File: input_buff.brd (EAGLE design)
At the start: 100 x 80 mm, 32 parts, among them X1 057-010-1, X2 057-016-1

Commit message: remains drc pass.
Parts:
- moved TP8 65.9 mm to (15.9, 2.54)
- moved TP7 63.1 mm to (14.6, 3.81)
- moved TP6 61.9 mm to (15.9, 5.08)
- moved TP5 59.1 mm to (14.6, 6.35)
- moved TP4 58.0 mm to (15.9, 7.62)
- moved TP3 55.3 mm to (14.6, 8.89)
- moved TP2 54.3 mm to (15.9, 10.2)
- moved TP1 51.7 mm to (14.6, 11.4)
- moved R3 14.8 mm to (19.7, 26.7)
- moved TP18 11.1 mm to (12.1, 26.7)
- moved TP17 6.25 mm to (31.1, 26.7)
- moved LED1 3.59 mm to (26.7, 26.7), turned to 180 degrees
- moved TP16 2.84 mm to (33.0, 3.81)
- moved R1 1.42 mm to (14.6, 20.3)
- moved R2 1.42 mm to (14.6, 15.2)
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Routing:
- net 1V8: track 6.19 -> 29.9 mm
- net IN_0: track 0.00 -> 22.5 mm
- net IN_1: track 0.00 -> 21.0 mm
- net OUT_0: track 0.00 -> 20.8 mm
- net OUT_6: track 0.00 -> 20.2 mm
- net IN_2: track 0.00 -> 19.8 mm
- net OUT_4: track 0.00 -> 19.7 mm
- net OUT_2: track 0.00 -> 19.4 mm
- net IN_3: track 0.00 -> 18.7 mm
- net IN_4: track 0.00 -> 17.9 mm
- net OUT_7: track 0.00 -> 17.4 mm
- net IN_5: track 0.00 -> 17.1 mm
- net OUT_5: track 0.00 -> 16.9 mm
- net IN_7: track 0.00 -> 16.8 mm
- net OUT_1: track 0.00 -> 16.6 mm
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- added copper zone on layer 1, net GND
- added copper zone on layer 16, net GND
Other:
- board size 100 x 80 mm -> 101.3 x 81.3 mm
- board text added: "0"
- board text added: "1"
- board text added: "1V8"
- board text added: "2"
- board text added: "3"
- board text added: "4"
- board text added: "5"
- board text added: "6"
- board text added: "7"
- board text added: "VIN"

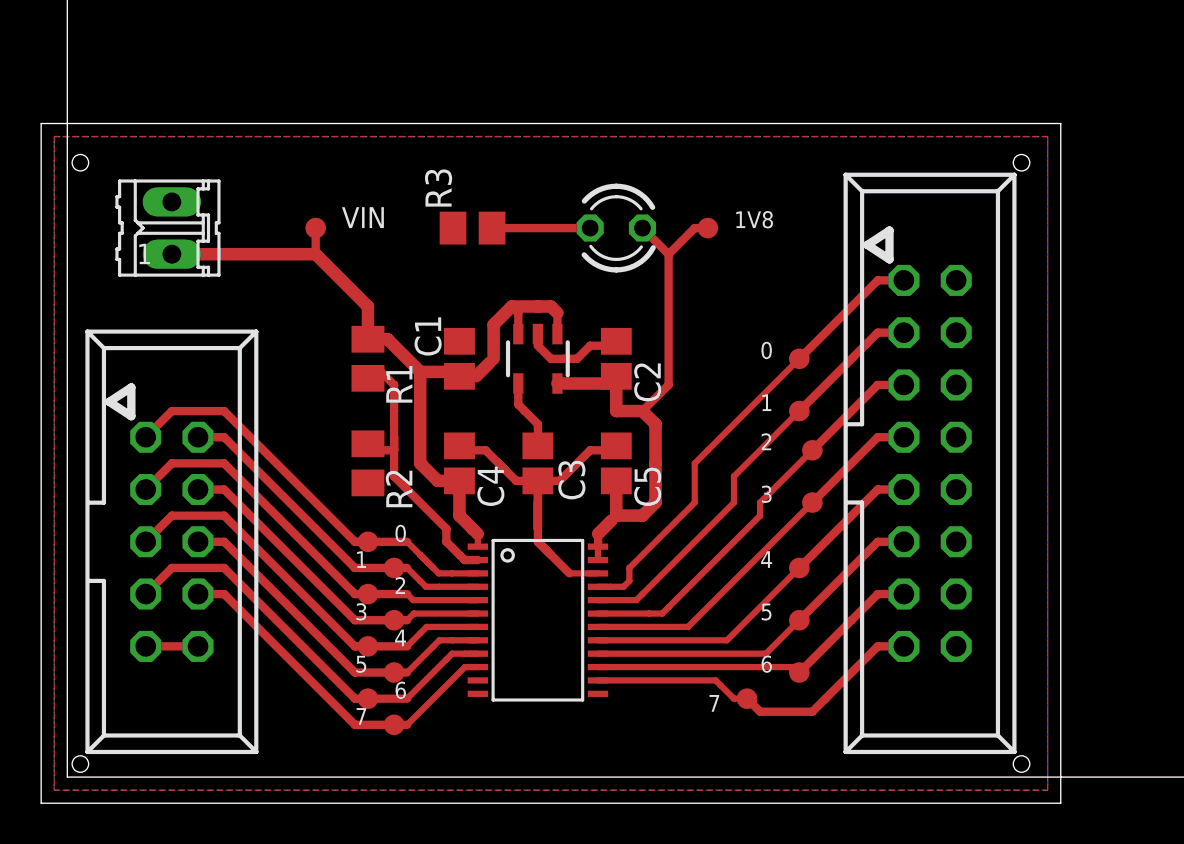
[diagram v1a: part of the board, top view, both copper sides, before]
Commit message: fusion pcb drc pass add two TP connected to 1V8 rail through a resistor, to be able to hack a pullup on an input signal "just in case".
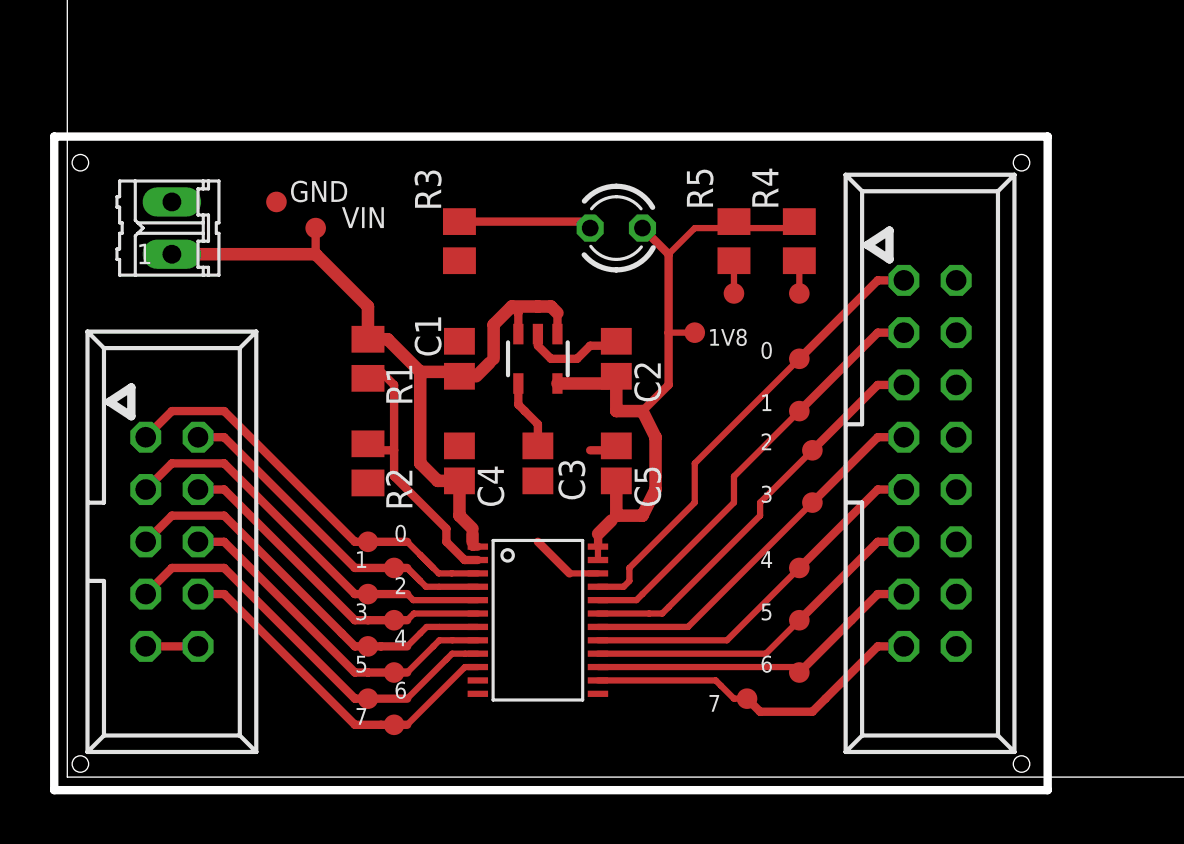
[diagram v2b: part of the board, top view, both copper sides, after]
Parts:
- added R4, R5: 4.7k, resistor:M0805
- added TP19, TP20, TP21: TPTP10R, testpad:TP10R
- moved TP17 5.12 mm to (30.5, 21.6)
- moved R3 0.90 mm to (19.1, 26.0), turned to 90 degrees
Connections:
- new net N$1: R4.1, TP20.TP
- new net N$4: R5.1, TP21.TP
- net 1V8: now also R4.2, R5.2
- net GND: now also TP19.TP
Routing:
- net GND: track 29.1 -> 12.4 mm
- net 1V8: track 29.9 -> 36.3 mm
- net OUT_1: track 16.6 -> 19.0 mm
- net N$4: track 0.00 -> 1.90 mm
- net N$3: track 4.76 -> 6.48 mm
- net N$1: track 0.00 -> 1.59 mm
- net OUT_4: track 19.7 -> 21.2 mm
- net OUT_5: track 16.9 -> 18.1 mm
- net OUT_3: track 16.4 -> 17.6 mm
- net OUT_7: track 17.4 -> 18.0 mm
- net OUT_6: track 20.2 -> 20.8 mm
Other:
- board size 101.3 x 81.3 mm -> 100.6 x 80.6 mm
- board text added: "GND"
